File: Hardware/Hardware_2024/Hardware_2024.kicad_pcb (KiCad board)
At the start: 2 copper layers, 94 x 54.6 mm, 45 parts, among them U1 Raspberry_Pi, U2 OKI, U3 TSR_1-2450

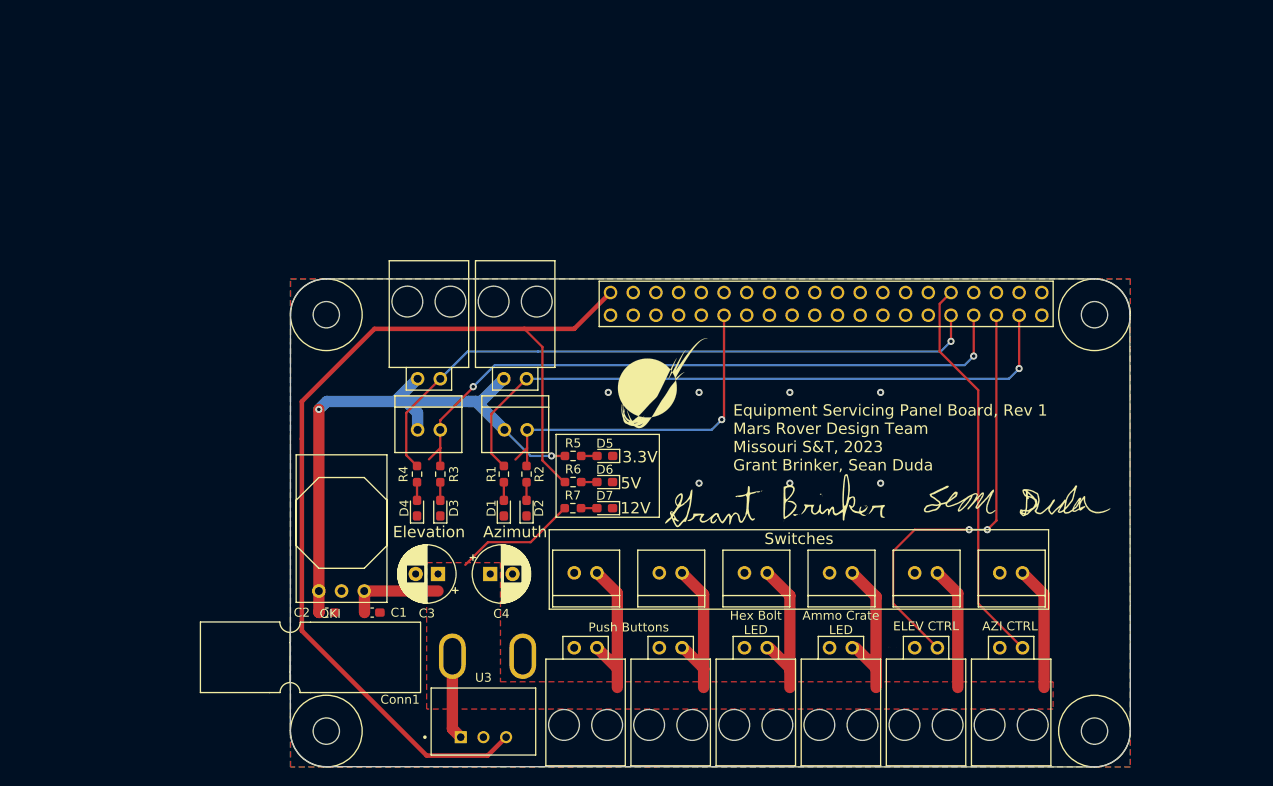
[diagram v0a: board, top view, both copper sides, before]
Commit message: assigned footprints worked on layout
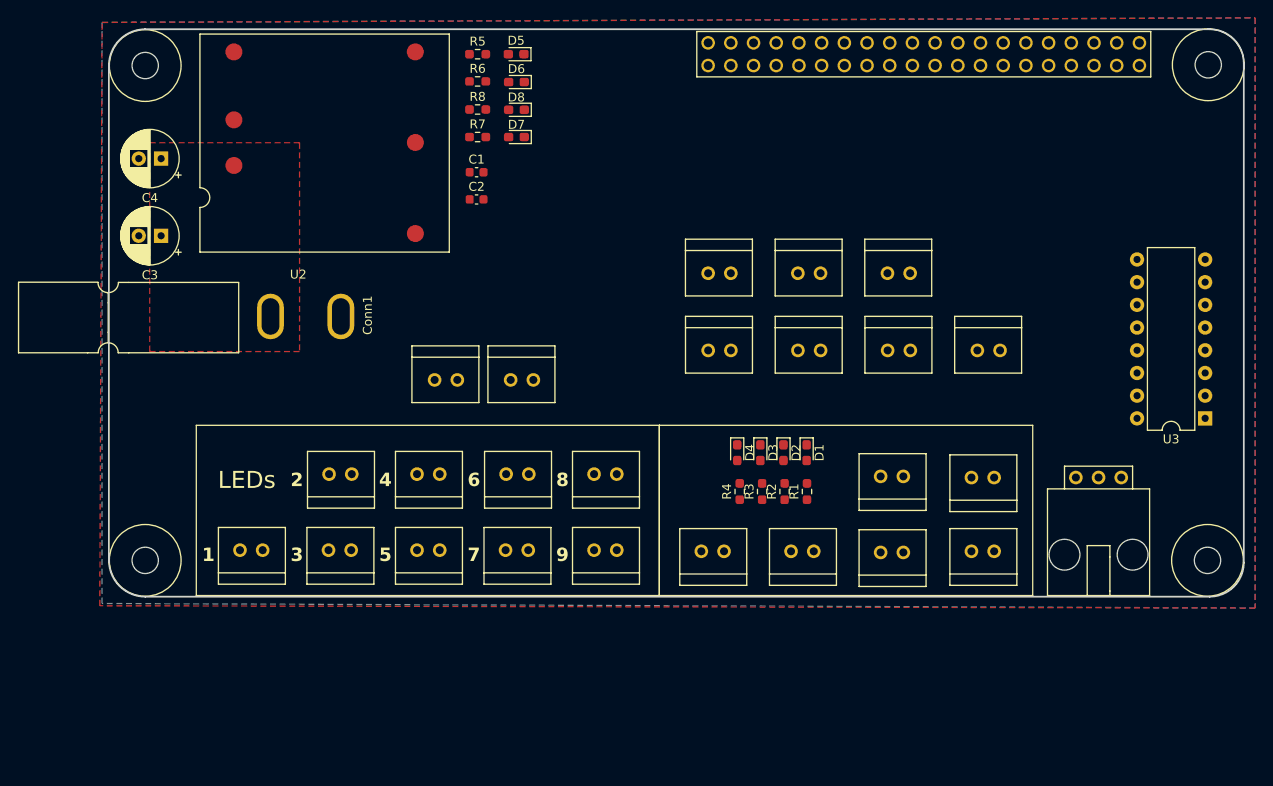
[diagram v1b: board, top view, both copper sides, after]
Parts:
- removed G***: LOGO, MRDT_Silkscreens:Sean_Duda_Signature_41.0mmx30.7mm
- removed G***: LOGO, MRDT_Silkscreens:z_sig_Grant_Brinker_25mmx6
- removed G***: LOGO, MRDT_Silkscreens:0_MRDT_Logo_10mm
- added Conn18: Molex_SL_02, MRDT_Connectors:MOLEX_SL_02_Vertical, F.Cu at (93.2, 113.3)
- added Conn19: Molex_SL_02, MRDT_Connectors:MOLEX_SL_02_Vertical, F.Cu at (93.2, 121.8)
- added Conn20: Molex_SL_02, MRDT_Connectors:MOLEX_SL_02_Vertical, F.Cu at (103.1, 113.3)
- added Conn21: Molex_SL_02, MRDT_Connectors:MOLEX_SL_02_Vertical, F.Cu at (103.1, 121.8)
- added Conn22: Molex_SL_02, MRDT_Connectors:MOLEX_SL_02_Vertical, F.Cu at (113.0, 113.3)
- added Conn23: Molex_SL_02, MRDT_Connectors:MOLEX_SL_02_Vertical, F.Cu at (113.0, 121.8)
- added Conn24: Molex_SL_02, MRDT_Connectors:MOLEX_SL_02_Vertical, F.Cu at (122.9, 113.3)
- added Conn25: Molex_SL_02, MRDT_Connectors:MOLEX_SL_02_Vertical, F.Cu at (122.9, 121.8)
- added Conn26: Molex_SL_03, MRDT_Connectors:MOLEX_SL_03_Horizontal, F.Cu at (179.3, 113.7)
- added D8: GREEN, LED_SMD:LED_0603_1608Metric_Pad1.05x0.95mm_HandSolder, F.Cu at (111.6, 72.5)
- added R8: 300, Resistor_SMD:R_0603_1608Metric_Pad0.98x0.95mm_HandSolder, F.Cu at (107.3, 72.5)
- C1, C2: footprint Capacitor_SMD:C_0603_1608Metric_Pad1.08x0.95mm_HandSolder -> Capacitor_SMD:C_0603_1608Metric
- Conn14, Conn16, Conn2, Conn3, Conn4, Conn5, Conn6, Conn7: footprint MRDT_Connectors:MOLEX_SL_02_Horizontal -> MRDT_Connectors:MOLEX_SL_02_Vertical
- U2: value OKI -> SHHD003A0A; footprint MRDT_Devices:OKI_Horizontal -> SHHD003A04A41:SHHD003A0A-SRZ
- U3: value TSR_1-2450 -> MCP3008; footprint MRDT_Devices:TSR_1-2433 -> Package_DIP:DIP-16_W7.62mm
- moved U3 87.6 mm to (188.7, 107.0), turned to 180 degrees
- moved Conn13 85.1 mm to (83.2, 121.8)
- moved Conn15 65.9 mm to (165.1, 121.9), turned to 180 degrees
- moved Conn14 65.5 mm to (165.1, 113.7), turned to 180 degrees
- moved C4 59.3 mm to (71.9, 78.0), turned to 180 degrees
- moved C1 50.6 mm to (107.2, 79.5)
- moved C2 49.2 mm to (107.2, 82.5)
- moved C3 48.9 mm to (71.9, 86.6)
- moved Conn16 48.7 mm to (154.9, 122.0), turned to 180 degrees
- moved Conn8 46.7 mm to (153.2, 90.8), turned to 0 degrees
- moved R5 46.2 mm to (107.3, 66.3)
- moved R6 46.1 mm to (107.3, 69.3)
- moved D5 46.0 mm to (111.6, 66.3)
- moved D6 45.8 mm to (111.6, 69.4)
- moved Conn17 44.9 mm to (154.9, 113.5), turned to 180 degrees
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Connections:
- C2 pad 1: +3V3 -> +5V
- Conn10 pad 1: +12V -> +3.3V
- Conn10 pad 2: GND -> Sw5
- Conn11 pad 1: +12V -> +3.3V
- Conn11 pad 2: GND -> Sw6
- Conn12 pad 1: +12V -> +3.3V
- Conn12 pad 2: GND -> Sw7
- Conn13 pad 2: GND -> LED1
- Conn4 pad 1: +12V -> +3.3V
- Conn4 pad 2: GND -> Button1
- Conn5 pad 1: +12V -> +3.3V
- Conn5 pad 2: GND -> Sw1
- Conn6 pad 1: +12V -> +3.3V
- Conn6 pad 2: GND -> Sw2
- Conn7 pad 1: +12V -> +3.3V
- Conn7 pad 2: GND -> Button2
- Conn8 pad 1: +12V -> +3.3V
- Conn8 pad 2: GND -> Sw3
- Conn9 pad 1: +12V -> +3.3V
- Conn9 pad 2: GND -> Sw4
- U1 pad 1: unconnected-(U1-Pad1) -> +3.3V
- U1 pad 10: unconnected-(U1-Pad10) -> LED2
- U1 pad 11: AZI_PLUS -> Sw4
- U1 pad 12: unconnected-(U1-Pad12) -> LED3
- U1 pad 13: unconnected-(U1-Pad13) -> Sw5
- U1 pad 15: unconnected-(U1-Pad15) -> Sw6
- U1 pad 16: unconnected-(U1-Pad16) -> LED4
- U1 pad 17: unconnected-(U1-Pad17) -> +3.3V
- U1 pad 18: (no net) -> LED5
- U1 pad 19: unconnected-(U1-Pad19) -> DIN
- U1 pad 21: unconnected-(U1-Pad21) -> DOUT
- U1 pad 22: unconnected-(U1-Pad22) -> LED6
- U1 pad 23: unconnected-(U1-Pad23) -> CLK
- U1 pad 24: unconnected-(U1-Pad24) -> CS
- U1 pad 26: unconnected-(U1-Pad26) -> LED7
- U1 pad 27: unconnected-(U1-Pad27) -> Sw7
- U1 pad 28: unconnected-(U1-Pad28) -> LED8
- U1 pad 29: unconnected-(U1-Pad29) -> AZI_PLUS
- U1 pad 3: unconnected-(U1-Pad3) -> Sw1
- U1 pad 33: ELEV_MINUS -> ELEV_CNTRL
- U1 pad 35: ELEV_CNTRL -> ELEV_MINUS
- U1 pad 36: unconnected-(U1-Pad36) -> LED9
- U1 pad 38: unconnected-(U1-Pad38) -> Button2
- U1 pad 4: unconnected-(U1-Pad4) -> +5V
- U1 pad 40: unconnected-(U1-Pad40) -> Button1
- U1 pad 5: unconnected-(U1-Pad5) -> Sw2
- U1 pad 7: unconnected-(U1-Pad7) -> Sw3
- U1 pad 8: unconnected-(U1-Pad8) -> LED1
- U2 pad 3: +3V3 -> GND
- U3 pad 1: +12V -> Net-(U3-CH0)
- U3 pad 2: GND -> unconnected-(U3-CH1-Pad2)
- U3 pad 3: +5V -> unconnected-(U3-CH2-Pad3)
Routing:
- net +12V: track 130.2 -> 0.00 mm
- net +5V: track 113.8 -> 0.00 mm
- net ELEV_MINUS: track 74.2 -> 0.00 mm, vias 2 -> 0
- net ELEV_PLUS: track 73.6 -> 0.00 mm, vias 1 -> 0
- net AZI_MINUS: track 73.5 -> 0.00 mm, vias 1 -> 0
- net +3V3: track 65.5 -> 0.00 mm, vias 2 -> 0
- net ELEV_CNTRL: track 48.8 -> 0.00 mm, vias 2 -> 0
- net AZI_CNTRL: track 44.1 -> 0.00 mm
- net AZI_PLUS: track 40.0 -> 0.00 mm, vias 1 -> 0
- net Net-(D4-A): track 2.02 -> 0.00 mm
- net Net-(D3-A): track 2.02 -> 0.00 mm
- net Net-(D2-A): track 2.02 -> 0.00 mm
- net Net-(D1-A): track 2.02 -> 0.00 mm
- net Net-(D7-A): track 1.78 -> 0.00 mm
- net Net-(D5-A): track 1.77 -> 0.00 mm
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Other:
- board size 94 x 54.6 mm -> 127 x 63.5 mm
- board text added: "1"
- board text added: "2"
- board text added: "3"
- board text added: "4"
- board text added: "5"
- board text added: "6"
- board text added: "7"
- board text added: "8"
- board text added: "9"
- board text added: "LEDs"
- board text removed: "12V"
- board text removed: "3.3V"
- board text removed: "5V"
- board text removed: "AZI CTRL"
- board text removed: "Ammo Crate LED"
- board text removed: "Azimuth"
- board text removed: "ELEV CTRL"
- board text removed: "Elevation"
- board text removed: "Equipment Servicing Panel Board, Rev 1 Mars Rover Design Team Missouri S&T, 2023 Grant Brinker, Sean Duda"
- board text removed: "Hex Bolt LED"
- board text removed: "Push Buttons"
- board text removed: "Switches"

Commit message: finished organizing. traces need work
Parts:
- removed D8: GREEN, LED_SMD:LED_0603_1608Metric_Pad1.05x0.95mm_HandSolder
- removed R8: 300, Resistor_SMD:R_0603_1608Metric_Pad0.98x0.95mm_HandSolder
- Conn26: footprint MRDT_Connectors:MOLEX_SL_03_Horizontal -> MRDT_Connectors:MOLEX_SL_03_Vertical
- moved Conn26 78.4 mm to (116.3, 67.1), turned to -90 degrees
- moved U3 77.6 mm to (122.7, 66.2), turned to 0 degrees
- moved Conn8 60.1 mm to (97.4, 113.3), turned to -90 degrees
- moved Conn6 58.2 mm to (89.4, 113.3), turned to -90 degrees
- moved Conn5 56.3 mm to (81.4, 113.2), turned to -90 degrees
- moved D1 37.8 mm to (181.9, 111.7)
- moved R1 37.8 mm to (181.9, 116.0)
- moved Conn12 36.8 mm to (129.2, 113.3), turned to -90 degrees
- moved D2 36.7 mm to (178.3, 111.7)
- moved Conn4 36.7 mm to (137.7, 113.3), turned to -90 degrees
- moved R2 36.6 mm to (178.2, 116.0)
- moved Conn7 36.5 mm to (145.9, 113.3), turned to -90 degrees
- moved D3 35.8 mm to (174.8, 111.7)
- moved R3 35.6 mm to (174.7, 116.0)
- moved Conn11 34.9 mm to (121.2, 113.3), turned to -90 degrees
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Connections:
- Conn14 pad 1: +3V3 -> +3.3V
- Conn15 pad 1: +3V3 -> +3.3V
- Conn16 pad 1: +3V3 -> +3.3V
- Conn17 pad 1: +3V3 -> +3.3V
- R5 pad 1: +3V3 -> +3.3V
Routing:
- net +3.3V: track 0.00 -> 148.1 mm, vias 0 -> 1
- net +5V: track 0.00 -> 63.0 mm
- net CS: track 0.00 -> 47.0 mm, vias 0 -> 2
- net CLK: track 0.00 -> 37.3 mm, vias 0 -> 1
- net DOUT: track 0.00 -> 36.6 mm, vias 0 -> 1
- net DIN: track 0.00 -> 35.6 mm, vias 0 -> 1
- net +12V: track 0.00 -> 31.3 mm
- net ELEV_PLUS: track 0.00 -> 21.3 mm
- net ELEV_MINUS: track 0.00 -> 18.4 mm
- net AZI_PLUS: track 0.00 -> 15.1 mm
- net AZI_MINUS: track 0.00 -> 11.5 mm
- net Net-(U3-CH0): track 0.00 -> 7.77 mm
- net Net-(D6-A): track 0.00 -> 2.59 mm
- net Net-(D1-A): track 0.00 -> 2.57 mm
- net Net-(D2-A): track 0.00 -> 2.57 mm
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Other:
- board size 127 x 63.5 mm -> 127 x 57.9 mm
- board text added: "Azi +"
- board text added: "Azi -"
- board text added: "Azi Ctrl"
- board text added: "Button1"
- board text added: "Button2"
- board text added: "Buttons"
- board text added: "Elev +"
- board text added: "Elev -"
- board text added: "Elev Ctrl"
- board text added: "Joystick"
- board text added: "Switches"
- board text added: "Voltmeter"

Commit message: worked on traces a bit
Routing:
- net Button1: track 0.00 -> 90.9 mm, vias 0 -> 3
- net Button2: track 0.00 -> 78.3 mm, vias 0 -> 2
- net ELEV_CNTRL: track 0.00 -> 71.0 mm, vias 0 -> 2
- net LED9: track 0.00 -> 68.7 mm, vias 0 -> 4
- net ELEV_PLUS: track 21.3 -> 84.7 mm, vias 0 -> 2
- net AZI_CNTRL: track 0.00 -> 59.6 mm, vias 0 -> 3
- net +3.3V: track 148.1 -> 200.4 mm
- net ELEV_MINUS: track 18.4 -> 67.6 mm, vias 0 -> 3
- net CS: track 47.0 -> 0.00 mm, vias 2 -> 0
- net AZI_PLUS: track 15.1 -> 55.9 mm
- net AZI_MINUS: track 11.5 -> 50.9 mm
- net CLK: track 37.3 -> 0.00 mm, vias 1 -> 0
- net DOUT: track 36.6 -> 0.00 mm, vias 1 -> 0
- net DIN: track 35.6 -> 0.00 mm, vias 1 -> 0

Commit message: Finished traces
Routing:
- net LED1: track 0.00 -> 107.6 mm, vias 0 -> 4
- net Sw1: track 0.00 -> 100.6 mm, vias 0 -> 2
- net LED2: track 0.00 -> 98.6 mm, vias 0 -> 4
- net Sw2: track 0.00 -> 92.6 mm, vias 0 -> 2
- net LED3: track 0.00 -> 87.5 mm, vias 0 -> 2
- net Sw3: track 0.00 -> 87.3 mm, vias 0 -> 2
- net LED5: track 0.00 -> 87.2 mm, vias 0 -> 1
- net Sw4: track 0.00 -> 85.7 mm, vias 0 -> 2
- net LED4: track 0.00 -> 82.0 mm, vias 0 -> 2
- net Sw5: track 0.00 -> 79.9 mm, vias 0 -> 2
- net Sw7: track 0.00 -> 74.3 mm, vias 0 -> 3
- net LED6: track 0.00 -> 73.7 mm, vias 0 -> 4
- net Sw6: track 0.00 -> 72.8 mm, vias 0 -> 2
- net LED7: track 0.00 -> 70.3 mm, vias 0 -> 3
- net LED8: track 0.00 -> 64.0 mm, vias 0 -> 3
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
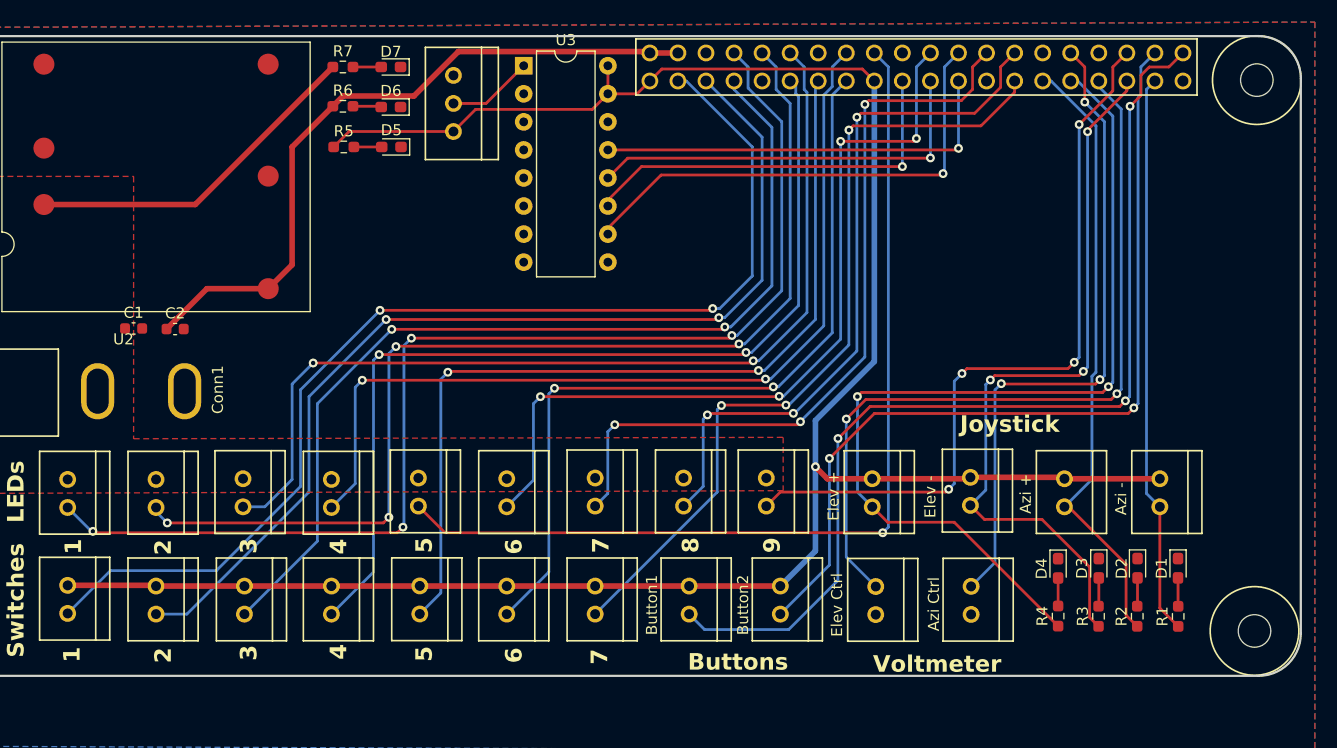
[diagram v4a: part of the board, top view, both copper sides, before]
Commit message: Added some vias
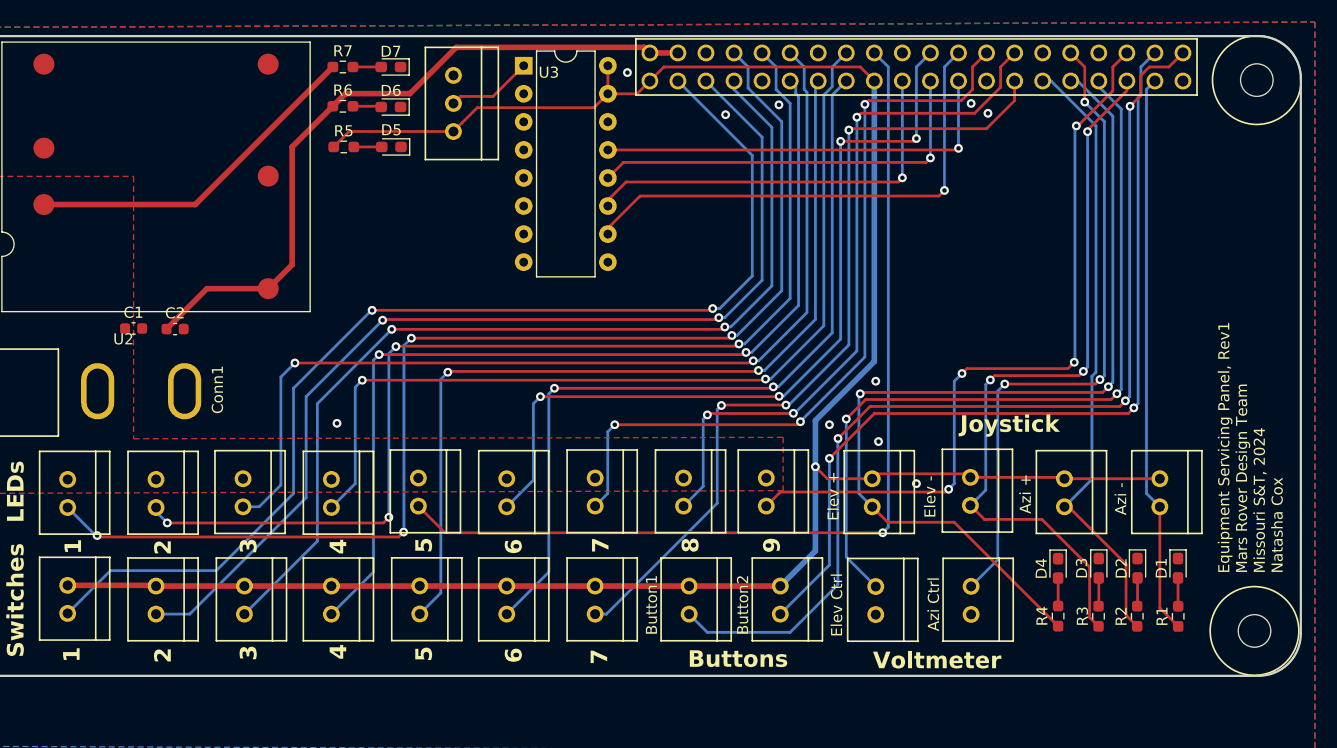
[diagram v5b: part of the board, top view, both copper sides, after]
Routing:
- net Sw7: track 74.3 -> 75.4 mm
- net CS: track 44.4 -> 45.4 mm
- net LED3: track 87.5 -> 88.2 mm
- net LED1: track 107.6 -> 108.2 mm
- net DIN: track 36.2 -> 36.8 mm
- net +3.3V: track 200.4 -> 200.9 mm
- net GND: vias 0 -> 10
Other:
- board text added: "Equipment Servicing Panel, Rev1 Mars Rover Design Team Missouri S&T, 2024 Natasha Cox"
